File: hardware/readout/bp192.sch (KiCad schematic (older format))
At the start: 6 parts

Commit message: Schematic progress
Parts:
- removed R? (x4): 10k, Resistor_SMD:R_1206_3216Metric_Pad1.42x1.75mm_HandSolder, symbol Device:R_Small
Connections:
- net labels added: BIAS10, BIAS11, BIAS12, BIAS5, BIAS6, BIAS7, BIAS8, BIAS9, BIAS[1..12], SIPM10, SIPM100, SIPM101, SIPM102, SIPM103, SIPM104, SIPM105, SIPM106, SIPM107, SIPM108, SIPM109, SIPM11, SIPM110, SIPM111, SIPM112, SIPM113, SIPM114, SIPM115, SIPM116, SIPM117, SIPM118, SIPM119, SIPM12, SIPM120, SIPM121, SIPM122, SIPM123, SIPM124, SIPM125, SIPM126, SIPM127, SIPM128, SIPM129, SIPM13, SIPM130, SIPM131, SIPM132, SIPM133, SIPM134, SIPM135, SIPM136, SIPM137, SIPM138, SIPM139, SIPM14, SIPM140, SIPM141, SIPM142, SIPM143, SIPM144, SIPM145, SIPM146, SIPM147, SIPM148, SIPM149, SIPM15, SIPM150, SIPM151, SIPM152, SIPM153, SIPM154, SIPM155, SIPM156, SIPM157, SIPM158, SIPM159, SIPM16, SIPM160, SIPM161, SIPM162, SIPM163, SIPM164, SIPM165, SIPM166, SIPM167, SIPM168, SIPM169, SIPM17, SIPM170, SIPM171, SIPM172, SIPM173, SIPM174, SIPM175, SIPM176, SIPM177, SIPM178, SIPM179, SIPM18, SIPM180, SIPM181, SIPM182, SIPM183, SIPM184, SIPM185, SIPM186, SIPM187, SIPM188, SIPM189, SIPM19, SIPM190, SIPM191, SIPM2, SIPM20, SIPM21, SIPM22, SIPM23, SIPM24, SIPM25, SIPM26, SIPM27, SIPM28, SIPM29, SIPM3, SIPM30, SIPM31, SIPM32, SIPM33, SIPM34, SIPM35, SIPM36, SIPM37, SIPM38, SIPM39, SIPM4, SIPM40, SIPM41, SIPM42, SIPM43, SIPM44, SIPM45, SIPM46, SIPM47, SIPM48, SIPM49, SIPM5, SIPM50, SIPM51, SIPM52, SIPM53, SIPM54, SIPM55, SIPM56, SIPM57, SIPM58, SIPM59, SIPM6, SIPM60, SIPM61, SIPM62, SIPM63, SIPM64, SIPM65, SIPM66, SIPM67, SIPM68, SIPM69, SIPM7, SIPM70, SIPM71, SIPM72, SIPM73, SIPM74, SIPM75, SIPM76, SIPM77, SIPM78, SIPM79, SIPM8, SIPM80, SIPM81, SIPM82, SIPM83, SIPM84, SIPM85, SIPM86, SIPM87, SIPM88, SIPM89, SIPM9, SIPM90, SIPM91, SIPM92, SIPM93, SIPM94, SIPM95, SIPM96, SIPM97, SIPM98, SIPM99, SIPM[0..191], SIPM[0..31], SIPM[113..127], SIPM[128..159], SIPM[160..191], SIPM[32..63], SIPM[64..80], SIPM[81..95], SIPM[96..112], TEMP1, TEMP2, TEMP3, TEMP[1..4], VDD
- net labels removed: 3.3V_SFP, BIAS[1..4], SIPM[0..575], SIPM_IN_A0, SIPM_IN_A1, SIPM_IN_A10, SIPM_IN_A11, SIPM_IN_A12, SIPM_IN_A13, SIPM_IN_A14, SIPM_IN_A15, SIPM_IN_A16, SIPM_IN_A17, SIPM_IN_A18, SIPM_IN_A19, SIPM_IN_A2, SIPM_IN_A20, SIPM_IN_A21, SIPM_IN_A22, SIPM_IN_A23, SIPM_IN_A24, SIPM_IN_A25, SIPM_IN_A26, SIPM_IN_A27, SIPM_IN_A28, SIPM_IN_A29, SIPM_IN_A3, SIPM_IN_A30, SIPM_IN_A31, SIPM_IN_A4, SIPM_IN_A5, SIPM_IN_A6, SIPM_IN_A7, SIPM_IN_A8, SIPM_IN_A9, SIPM_IN_B0, SIPM_IN_B1, SIPM_IN_B10, SIPM_IN_B11, SIPM_IN_B12, SIPM_IN_B13, SIPM_IN_B14, SIPM_IN_B15, SIPM_IN_B16, SIPM_IN_B17, SIPM_IN_B18, SIPM_IN_B19, SIPM_IN_B2, SIPM_IN_B20, SIPM_IN_B21, SIPM_IN_B22, SIPM_IN_B23, SIPM_IN_B24, SIPM_IN_B25, SIPM_IN_B26, SIPM_IN_B27, SIPM_IN_B28, SIPM_IN_B29, SIPM_IN_B3, SIPM_IN_B30, SIPM_IN_B31, SIPM_IN_B4, SIPM_IN_B5, SIPM_IN_B6, SIPM_IN_B7, SIPM_IN_B8, SIPM_IN_B9, SIPM_TEMP
- wire segments 252 -> 361
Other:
- moved on the sheet: J?

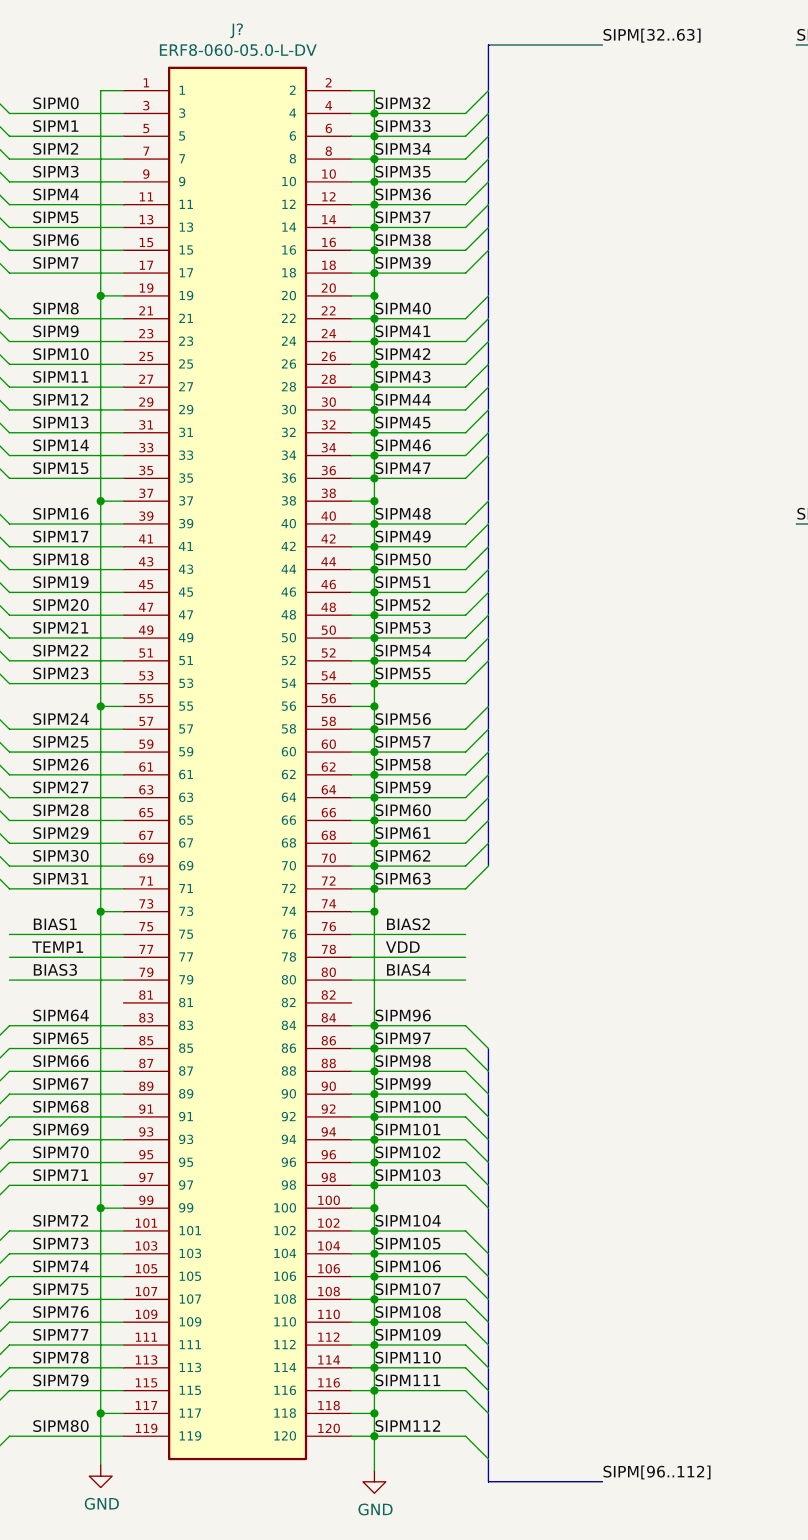
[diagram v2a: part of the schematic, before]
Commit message: Readout schem heirarchy almost done
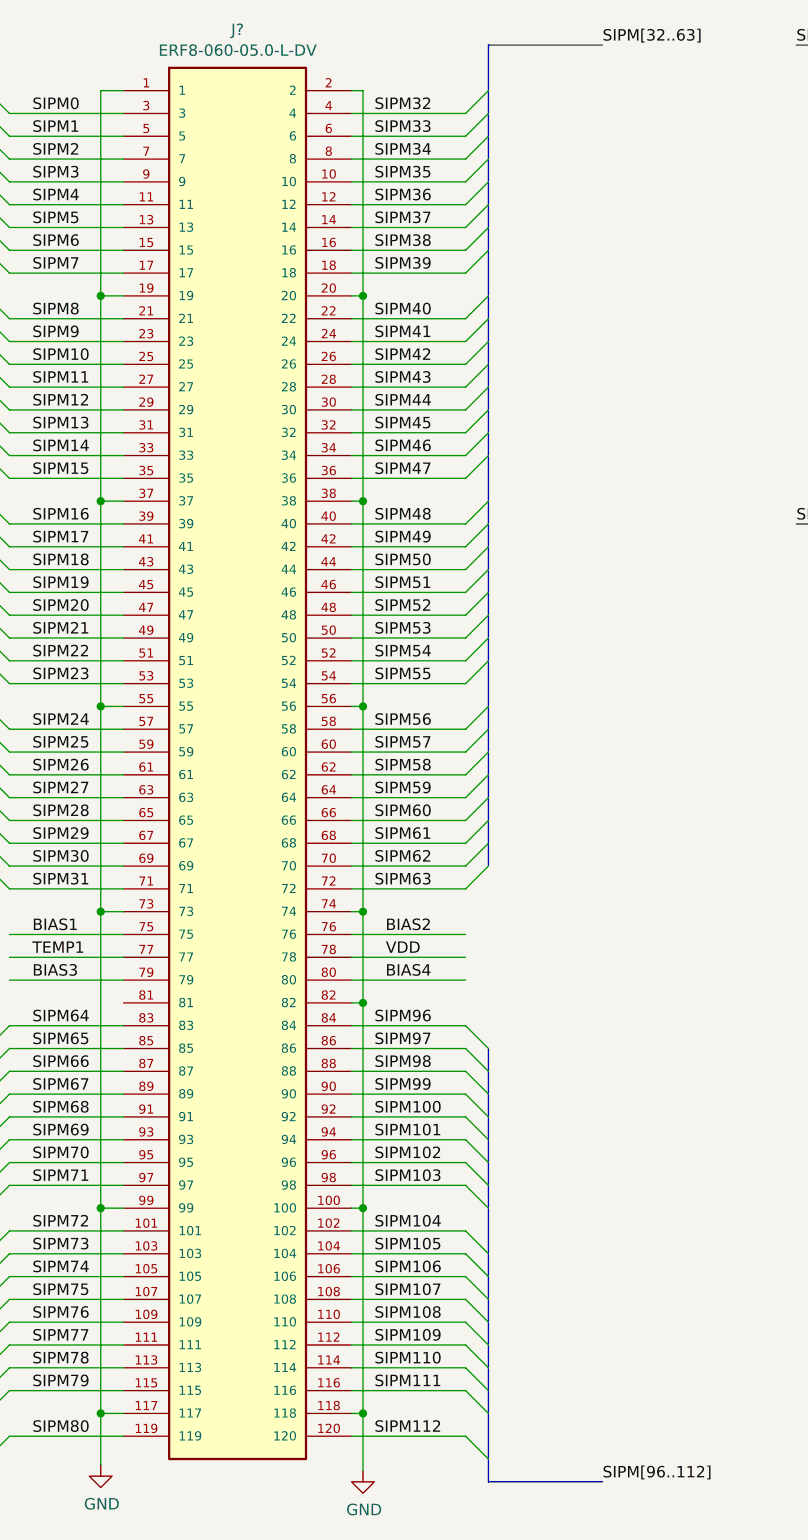
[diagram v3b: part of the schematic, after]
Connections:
- wire segments 361 -> 265

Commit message: schematic in progress
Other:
- note added: "EMPHATIC readout board\nBackplane connector pair (1 of 3)"
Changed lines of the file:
@@
 $Descr User 11000 9000
 encoding utf-8
-Sheet 2 35
+Sheet 2 38
 Title ""
 Date ""
@@
 Wire Bus Line
 	2650 750  2650 4350
+Text Notes 6450 7600 0    75   ~ 0
+EMPHATIC readout board\nBackplane connector pair (1 of 3)
 $EndSCHEMATC

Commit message: working on schematic
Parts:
- gave numbers to parts that had none: 2
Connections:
- net labels added: +1V8, BIAS, TEMP[1..3]
- net labels removed: BIAS1, BIAS10, BIAS11, BIAS12, BIAS2, BIAS3, BIAS4, BIAS5, BIAS6, BIAS7, BIAS8, BIAS9, BIAS[1..12], TEMP[1..4], VDD
- wire segments 265 -> 257
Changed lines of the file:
@@
 AR Path="/611127F4/611924E5/61123729" Ref="J?"  Part="1"
 AR Path="/611127F4/61192572/61123729" Ref="J?"  Part="1"
-AR Path="/61195331/61123729" Ref="J?"  Part="1"
+AR Path="/61195331/61123729" Ref="J1"  Part="1"
 AR Path="/61195337/61123729" Ref="J?"  Part="1"
 AR Path="/6119533D/61123729" Ref="J?"  Part="1"
-AR Path="/61119E87/61123729" Ref="J?"  Part="1"
-AR Path="/6111A883/61123729" Ref="J?"  Part="1"
-F 0 "J?" H 3750 7117 50  0000 C CNN
+AR Path="/61119E87/61123729" Ref="J5"  Part="1"
+AR Path="/6111A883/61123729" Ref="J9"  Part="1"
+F 0 "J9" H 3750 7117 50  0000 C CNN
 F 1 "ERF8-060-05.0-L-DV" H 3750 7026 50  0000 C CNN
 F 2 "" H 3750 3900 50  0001 C CNN
@@
 AR Path="/611127F4/611924E5/6112374B" Ref="#PWR?"  Part="1"
 AR Path="/611127F4/61192572/6112374B" Ref="#PWR?"  Part="1"
-AR Path="/61195331/6112374B" Ref="#PWR?"  Part="1"
+AR Path="/61195331/6112374B" Ref="#PWR02"  Part="1"
 AR Path="/61195337/6112374B" Ref="#PWR?"  Part="1"
 AR Path="/6119533D/6112374B" Ref="#PWR?"  Part="1"
-AR Path="/61119E87/6112374B" Ref="#PWR?"  Part="1"
-AR Path="/6111A883/6112374B" Ref="#PWR?"  Part="1"
-F 0 "#PWR?" H 4300 6750 50  0001 C CNN
+AR Path="/61119E87/6112374B" Ref="#PWR0155"  Part="1"
+AR Path="/6111A883/6112374B" Ref="#PWR0308"  Part="1"
+F 0 "#PWR0308" H 4300 6750 50  0001 C CNN
 F 1 "GND" H 4305 6827 50  0000 C CNN
 F 2 "" H 4300 7000 50  0001 C CNN
@@
 AR Path="/611127F4/611924E5/61123751" Ref="#PWR?"  Part="1"
 AR Path="/611127F4/61192572/61123751" Ref="#PWR?"  Part="1"
-AR Path="/61195331/61123751" Ref="#PWR?"  Part="1"
+AR Path="/61195331/61123751" Ref="#PWR01"  Part="1"
 AR Path="/61195337/61123751" Ref="#PWR?"  Part="1"
 AR Path="/6119533D/61123751" Ref="#PWR?"  Part="1"
-AR Path="/61119E87/61123751" Ref="#PWR?"  Part="1"
-AR Path="/6111A883/61123751" Ref="#PWR?"  Part="1"
-F 0 "#PWR?" H 3150 6725 50  0001 C CNN
+AR Path="/61119E87/61123751" Ref="#PWR0154"  Part="1"
+AR Path="/6111A883/61123751" Ref="#PWR0307"  Part="1"
+F 0 "#PWR0307" H 3150 6725 50  0001 C CNN
 F 1 "GND" H 3155 6802 50  0000 C CNN
 F 2 "" H 3150 6975 50  0001 C CNN
@@
 $EndComp
 Text Label 4600 4650 2    50   ~ 0
-BIAS2
+BIAS
 Text Label 4600 4850 2    50   ~ 0
-BIAS4
+BIAS
 Text Label 2850 4650 0    50   ~ 0
-BIAS1
+BIAS
 Text Label 2850 4850 0    50   ~ 0
-BIAS3
+BIAS
 $Comp
 L readout:ERF8-060-05.0-L-DV J?
@@
 AR Path="/611127F4/611924E5/6112D059" Ref="J?"  Part="1"
 AR Path="/611127F4/61192572/6112D059" Ref="J?"  Part="1"
-AR Path="/61195331/6112D059" Ref="J?"  Part="1"
+AR Path="/61195331/6112D059" Ref="J2"  Part="1"
 AR Path="/61195337/6112D059" Ref="J?"  Part="1"
 AR Path="/6119533D/6112D059" Ref="J?"  Part="1"
-AR Path="/61119E87/6112D059" Ref="J?"  Part="1"
-AR Path="/6111A883/6112D059" Ref="J?"  Part="1"
-F 0 "J?" H 7800 7217 50  0000 C CNN
+AR Path="/61119E87/6112D059" Ref="J6"  Part="1"
+AR Path="/6111A883/6112D059" Ref="J10"  Part="1"
+F 0 "J10" H 7800 7217 50  0000 C CNN
 F 1 "ERF8-060-05.0-L-DV" H 7800 7126 50  0000 C CNN
 F 2 "" H 7800 4000 50  0001 C CNN
@@
 	7300 2750 6900 2750
 Wire Wire Line
-	8300 2750 8800 2750
+	8300 2750 8650 2750
 Text Label 8450 2750 0    50   ~ 0
-BIAS6
+BIAS
 Text Label 6950 2750 0    50   ~ 0
-BIAS5
+BIAS
 Wire Wire Line
 	7300 2850 6900 2850
@@
 TEMP2
 Text Label 6950 2950 0    50   ~ 0
-BIAS7
-Text Label 8450 2850 0    50   ~ 0
-VDD
+BIAS
 Text Label 8450 2950 0    50   ~ 0
-BIAS8
+BIAS
 Wire Wire Line
 	7300 6650 7250 6650
@@
 	8300 6750 8800 6750
 Wire Wire Line
-	8300 6850 8800 6850
-Wire Wire Line
 	8300 6950 8800 6950
 Wire Wire Line
@@
 	2750 4650 3250 4650
 Wire Wire Line
-	4250 4750 4750 4750
-Wire Wire Line
 	4250 4650 4750 4650
 Wire Wire Line
 	4250 4850 4750 4850
-Text Label 4400 4750 0    50   ~ 0
-VDD
 Text Label 2850 4750 0    50   ~ 0
 TEMP1
@@
 	3250 4750 2750 4750
 Text Label 6900 6750 0    50   ~ 0
-BIAS9
+BIAS
 Text Label 8400 6750 0    50   ~ 0
-BIAS10
+BIAS
 Text Label 6900 6950 0    50   ~ 0
-BIAS11
+BIAS
 Text Label 8400 6950 0    50   ~ 0
-BIAS12
+BIAS
 Text Label 6900 6850 0    50   ~ 0
 TEMP3
-Text Label 8400 6850 0    50   ~ 0
-VDD
 Text HLabel 9800 3750 2    50   Output ~ 10
 SIPM[0..191]
@@
 Text Label 9250 3750 0    50   ~ 0
 SIPM[0..191]
-Entry Wire Line
-	1700 1250 1800 1350
-Entry Wire Line
-	1700 1350 1800 1450
-Entry Wire Line
-	1700 1450 1800 1550
-Entry Wire Line
-	1700 1550 1800 1650
-Entry Wire Line
-	1700 1650 1800 1750
-Entry Wire Line
-	1700 1750 1800 1850
-Entry Wire Line
-	1700 1850 1800 1950
-Entry Wire Line
-	1700 1950 1800 2050
-Entry Wire Line
-	1700 2050 1800 2150
-Entry Wire Line
-	1700 2150 1800 2250
-Entry Wire Line
-	1700 2250 1800 2350
-Entry Wire Line
-	1700 2350 1800 2450
-Wire Wire Line
-	1800 1350 2300 1350
-Wire Wire Line
-	1800 1450 2300 1450
-Wire Wire Line
-	1800 1550 2300 1550
-Wire Wire Line
-	1800 1650 2300 1650
-Wire Wire Line
-	1800 1750 2300 1750
-Wire Wire Line
-	1800 1850 2300 1850
-Wire Wire Line
-	1800 1950 2300 1950
-Wire Wire Line
-	1800 2050 2300 2050
-Wire Wire Line
-	1800 2150 2300 2150
-Wire Wire Line
-	1800 2250 2300 2250
-Wire Wire Line
-	1800 2350 2300 2350
-Wire Wire Line
-	1800 2450 2300 2450
-Text Label 1900 1350 0    50   ~ 0
-BIAS1
-Text Label 1900 1450 0    50   ~ 0
-BIAS2
-Text Label 1900 1550 0    50   ~ 0
-BIAS3
-Text Label 1900 1650 0    50   ~ 0
-BIAS4
-Text Label 1900 1750 0    50   ~ 0
-BIAS5
-Text Label 1900 1850 0    50   ~ 0
-BIAS6
-Text Label 1900 1950 0    50   ~ 0
-BIAS7
-Text Label 1900 2050 0    50   ~ 0
-BIAS8
-Text Label 1900 2150 0    50   ~ 0
-BIAS9
-Text Label 1900 2250 0    50   ~ 0
-BIAS10
-Text Label 1900 2350 0    50   ~ 0
-BIAS11
-Text Label 1900 2450 0    50   ~ 0
-BIAS12
-Wire Bus Line
-	1200 1050 1700 1050
-Text Label 1250 1050 0    50   ~ 0
-BIAS[1..12]
-Text HLabel 1200 750  0    50   Input ~ 0
-VDD
-Text HLabel 1200 1050 0    50   Input ~ 0
-BIAS[1..12]
-Wire Wire Line
-	1200 750  1700 750
-Text Label 1400 750  0    50   ~ 0
-VDD
 $Comp
 L power:GND #PWR?
@@
 AR Path="/611127F4/611924E5/612666AB" Ref="#PWR?"  Part="1"
 AR Path="/611127F4/61192572/612666AB" Ref="#PWR?"  Part="1"
-AR Path="/61195331/612666AB" Ref="#PWR?"  Part="1"
+AR Path="/61195331/612666AB" Ref="#PWR04"  Part="1"
 AR Path="/61195337/612666AB" Ref="#PWR?"  Part="1"
 AR Path="/6119533D/612666AB" Ref="#PWR?"  Part="1"
-AR Path="/61119E87/612666AB" Ref="#PWR?"  Part="1"
-AR Path="/6111A883/612666AB" Ref="#PWR?"  Part="1"
-F 0 "#PWR?" H 7250 6800 50  0001 C CNN
+AR Path="/61119E87/612666AB" Ref="#PWR0157"  Part="1"
+AR Path="/6111A883/612666AB" Ref="#PWR0310"  Part="1"
+F 0 "#PWR0310" H 7250 6800 50  0001 C CNN
 F 1 "GND" H 7350 7050 50  0000 C CNN
 F 2 "" H 7250 7050 50  0001 C CNN
@@
 AR Path="/611127F4/611924E5/6130A8CC" Ref="#PWR?"  Part="1"
 AR Path="/611127F4/61192572/6130A8CC" Ref="#PWR?"  Part="1"
-AR Path="/61195331/6130A8CC" Ref="#PWR?"  Part="1"
+AR Path="/61195331/6130A8CC" Ref="#PWR05"  Part="1"
 AR Path="/61195337/6130A8CC" Ref="#PWR?"  Part="1"
 AR Path="/6119533D/6130A8CC" Ref="#PWR?"  Part="1"
-AR Path="/61119E87/6130A8CC" Ref="#PWR?"  Part="1"
-AR Path="/6111A883/6130A8CC" Ref="#PWR?"  Part="1"
-F 0 "#PWR?" H 8350 6800 50  0001 C CNN
+AR Path="/61119E87/6130A8CC" Ref="#PWR0158"  Part="1"
+AR Path="/6111A883/6130A8CC" Ref="#PWR0311"  Part="1"
+F 0 "#PWR0311" H 8350 6800 50  0001 C CNN
 F 1 "GND" H 8450 7050 50  0000 C CNN
 F 2 "" H 8350 7050 50  0001 C CNN
@@
 Connection ~ 8350 6650
 Text HLabel 9800 4050 2    50   Output ~ 0
-TEMP[1..4]
+TEMP[1..3]
 Wire Bus Line
 	9800 4050 9200 4050
 Text Label 9250 4050 0    50   ~ 0
-TEMP[1..4]
+TEMP[1..3]
 Wire Wire Line
 	4250 1750 4750 1750
@@
 Text Notes 6450 7600 0    75   ~ 0
 EMPHATIC readout board\nBackplane connector pair (1 of 3)
+Text HLabel 1200 1100 0    50   Input ~ 0
+BIAS
+Wire Wire Line
+	1200 1100 1700 1100
+Text Label 1400 1100 0    50   ~ 0
+BIAS
+$Comp
+L power:+1V8 #PWR03
+U 1 1 61217EE1
+P 5050 4650
+AR Path="/61195331/61217EE1" Ref="#PWR03"  Part="1"
+AR Path="/61119E87/61217EE1" Ref="#PWR0156"  Part="1"
+AR Path="/6111A883/61217EE1" Ref="#PWR0309"  Part="1"
+F 0 "#PWR0309" H 5050 4500 50  0001 C CNN
+F 1 "+1V8" H 5065 4823 50  0000 C CNN
+F 2 "" H 5050 4650 50  0001 C CNN
+F 3 "" H 5050 4650 50  0001 C CNN
+	1    5050 4650
+	1    0    0    -1
+$EndComp
+Wire Wire Line
+	5050 4650 5050 4750
+Wire Wire Line
+	4250 4750 5050 4750
+$Comp
+L power:+1V8 #PWR06
+U 1 1 61236ED5
+P 9000 2700
+AR Path="/61195331/61236ED5" Ref="#PWR06"  Part="1"
+AR Path="/61119E87/61236ED5" Ref="#PWR0159"  Part="1"
+AR Path="/6111A883/61236ED5" Ref="#PWR0312"  Part="1"
+F 0 "#PWR0312" H 9000 2550 50  0001 C CNN
+F 1 "+1V8" H 9015 2873 50  0000 C CNN
+F 2 "" H 9000 2700 50  0001 C CNN
+F 3 "" H 9000 2700 50  0001 C CNN
+	1    9000 2700
+	1    0    0    -1
+$EndComp
+Wire Wire Line
+	8800 2850 8800 2700
+Wire Wire Line
+	8800 2700 9000 2700
+$Comp
+L power:+1V8 #PWR07
+U 1 1 61275F7C
+P 9100 6700
+AR Path="/61195331/61275F7C" Ref="#PWR07"  Part="1"
+AR Path="/61119E87/61275F7C" Ref="#PWR0160"  Part="1"
+AR Path="/6111A883/61275F7C" Ref="#PWR0313"  Part="1"
+F 0 "#PWR0313" H 9100 6550 50  0001 C CNN
+F 1 "+1V8" H 9115 6873 50  0000 C CNN
+F 2 "" H 9100 6700 50  0001 C CNN
+F 3 "" H 9100 6700 50  0001 C CNN
+	1    9100 6700
+	1    0    0    -1
+$EndComp
+Wire Wire Line
+	9100 6700 9100 6850
+Wire Wire Line
+	8300 6850 9100 6850
 Wire Bus Line
 	8900 750  8900 2450
@@
 	6700 750  6700 2450
 Wire Bus Line
-	1700 1050 1700 2350
-Wire Bus Line
 	4850 5150 4850 7050
